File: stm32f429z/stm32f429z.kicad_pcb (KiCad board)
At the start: 4 copper layers, 153 x 114.3 mm, 85 parts, among them J1 ADC connector 2, J10 UART 1 connectors, J11 CAN connector, J12 USB to UART GPIO, J13 USB_OTG, J14 I2C 1 connector, J15 GPIO, J16 GPIO, J2 ADC connector 1, J3 SPI 2 connector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

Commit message: updated some stuff
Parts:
- J6: footprint Connector_USB:USB_A_Molex_67643_Horizontal -> Connector_USB:USB_A_Wuerth_61400826021_Horizontal_Stacked
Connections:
- SW1 pad 1: BOOT0 -> +3.3V
- SW1 pad 2: +3.3V -> BOOT0
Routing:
- net GND: track 433.2 -> 417.8 mm, vias 73 -> 122
- net +5V: track 217.9 -> 214.6 mm
- net +3.3V: track 166.8 -> 165.6 mm
- net BOOT0: track 99.1 -> 99.9 mm
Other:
- board text added: "BOOTL"
- board text added: "NRST"
- board text added: "PROG"
- board text removed: "Boot0"

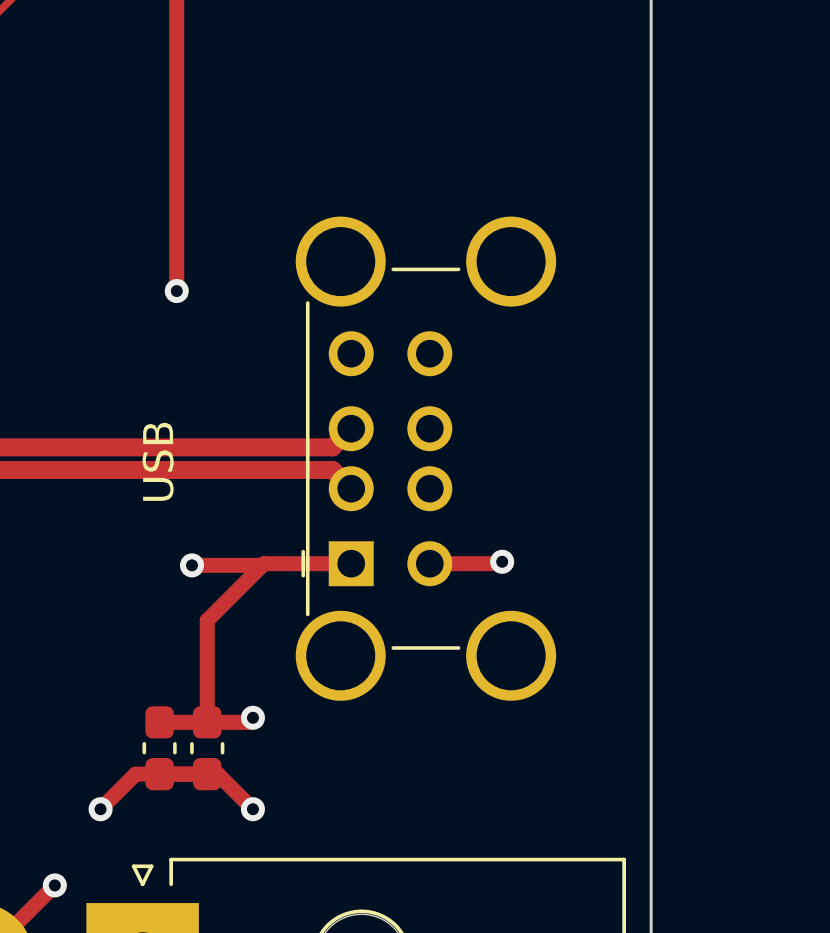
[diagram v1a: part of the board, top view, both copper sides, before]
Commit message: changed the usb A connector
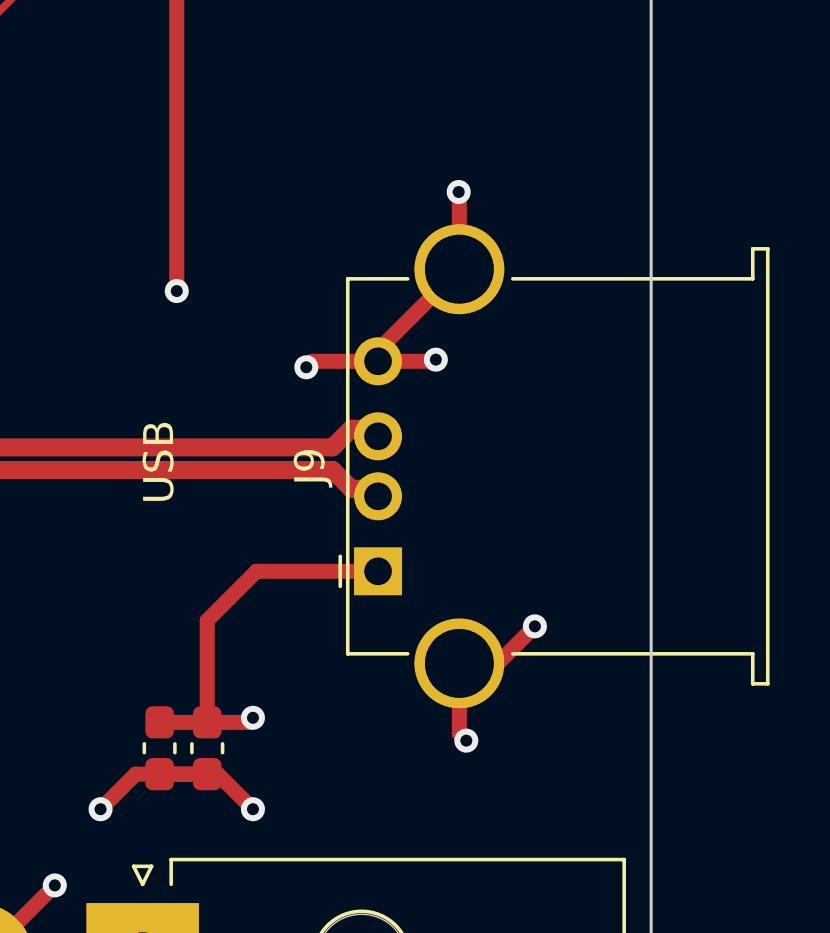
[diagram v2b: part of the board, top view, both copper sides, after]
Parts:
- removed J6: USB_OTG, Connector_USB:USB_A_Wuerth_61400826021_Horizontal_Stacked
- added J9: USB_A, Connector_USB:USB_A_Stewart_SS-52100-001_Horizontal, F.Cu at (211.9, 89.1)
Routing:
- net GND: track 417.8 -> 432.3 mm, vias 122 -> 126
- net +5V: track 214.6 -> 212.9 mm, vias 36 -> 35
- net USB_OTG_FS_DP-: track 49.9 -> 50.9 mm
- net USB_OTG_FS_DP+: track 49.9 -> 50.9 mm
